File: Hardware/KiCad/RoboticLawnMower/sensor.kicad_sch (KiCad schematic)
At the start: 7 parts, among them J19 RAIN, J20 Dist 00, J21 Dist 01, J22 Dist 02, J6 Coll 00, J7 Coll 01, J8 Coll 02

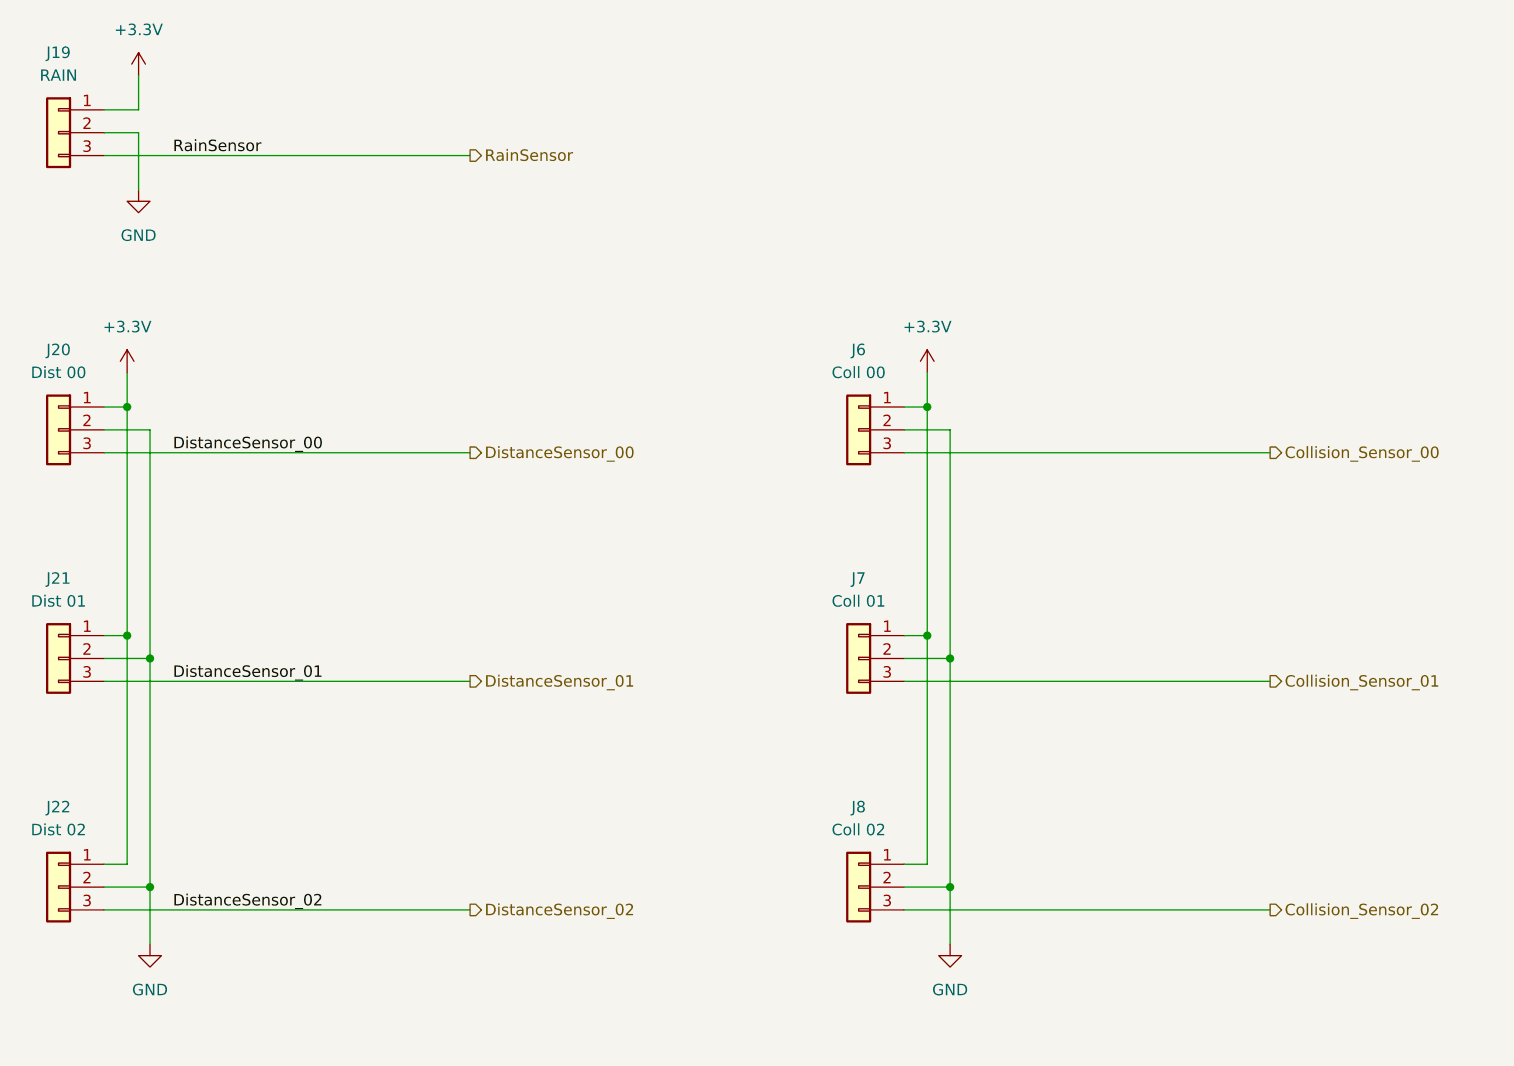
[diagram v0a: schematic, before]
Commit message: Redesign: - Controller - I2C pinning geändert - uvm
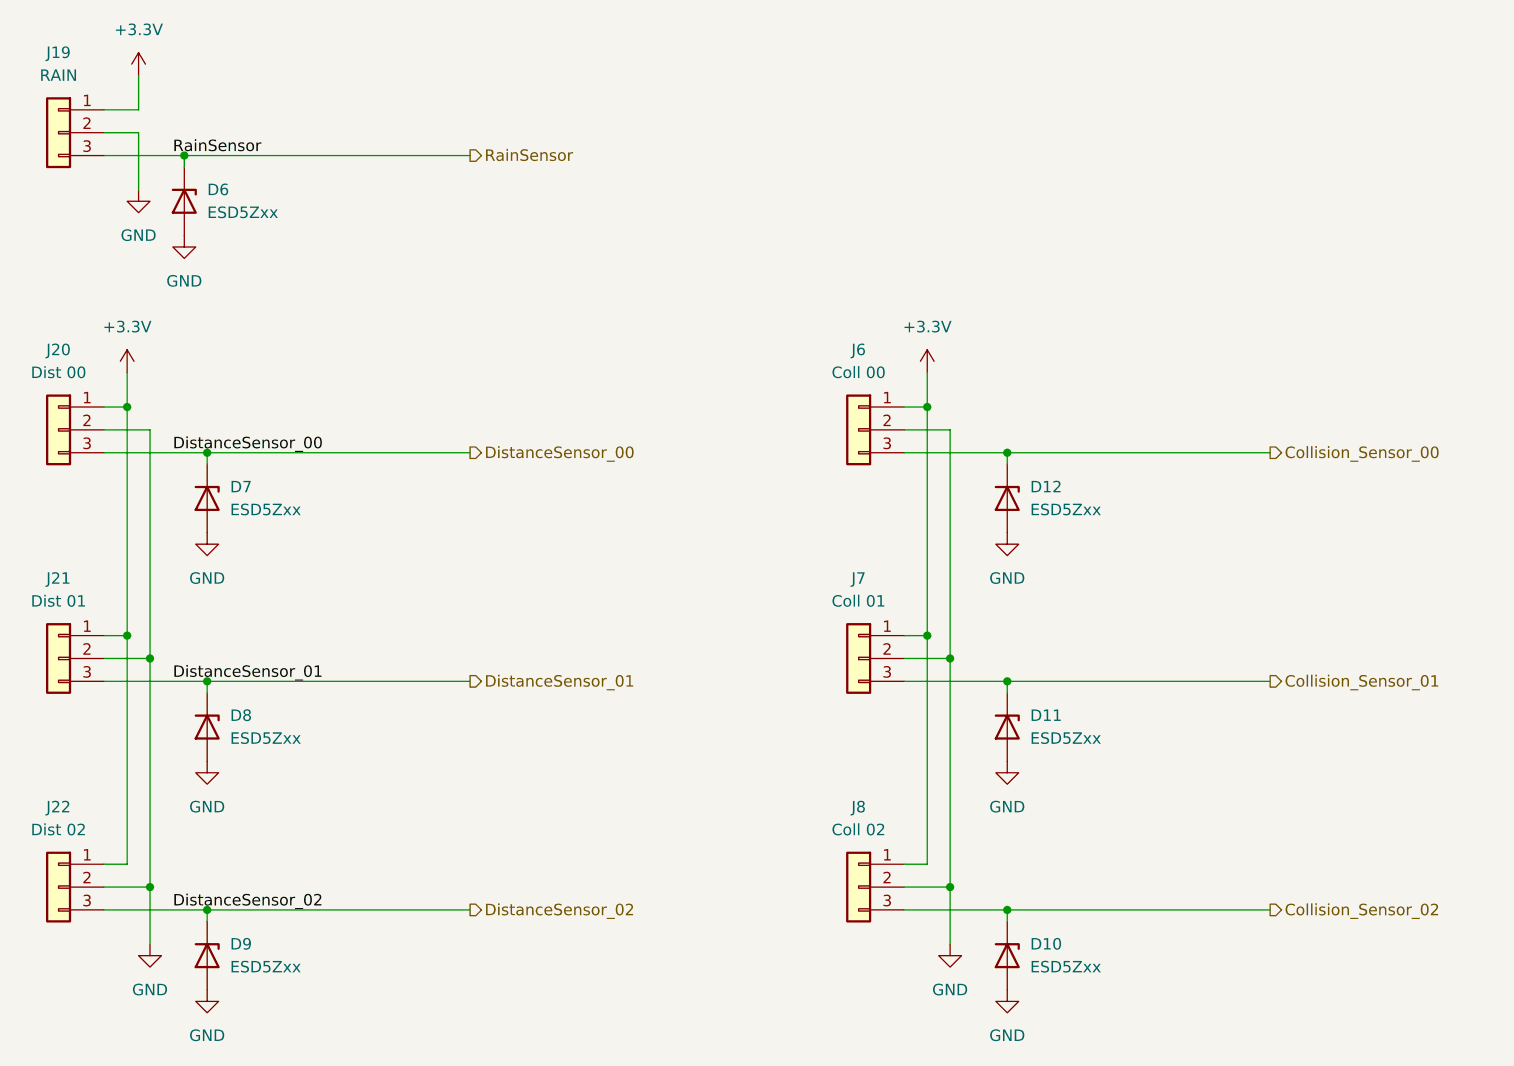
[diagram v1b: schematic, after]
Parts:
- added D10, D11, D12, D6, D7, D8, D9: ESD5Zxx, Diode_SMD:D_SOD-523, symbol Diode:ESD5Zxx
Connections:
- net Collision_Sensor_00: now also D12.1 (K)
- net Collision_Sensor_01: now also D11.1 (K)
- net Collision_Sensor_02: now also D10.1 (K)
- net DistanceSensor_00: now also D7.1 (K)
- net DistanceSensor_01: now also D8.1 (K)
- net DistanceSensor_02: now also D9.1 (K)
- net GND: now also D10.2 (A), D11.2 (A), D12.2 (A), D6.2 (A), D7.2 (A), D8.2 (A), D9.2 (A)
- net RainSensor: now also D6.1 (K)
